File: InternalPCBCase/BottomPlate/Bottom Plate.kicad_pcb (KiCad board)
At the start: 2 copper layers, 138.6 x 93.5 mm, 6 parts

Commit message: V1.01 PCB and Plates incl Gerbers
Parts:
- added SCREW7: MountingHole_2.2mm_M2_DIN965, Mounting_Holes:MountingHole_2.2mm_M2_DIN965, F.Cu at (128.5, 106.8)
- added SCREW8: MountingHole_2.2mm_M2_DIN965, Mounting_Holes:MountingHole_2.2mm_M2_DIN965, F.Cu at (154.9, 68.8)
- moved SCREW4 4.48 mm to (154.9, 106.8)
- moved SCREW3 1.35 mm to (128.5, 68.8)
- moved SCREW5 1.06 mm to (189.2, 72.2)
- moved SCREW6 0.58 mm to (184.8, 109.2)
- moved SCREW1 0.24 mm to (94.0, 72.2)
- moved SCREW2 0.14 mm to (94.0, 110.3)
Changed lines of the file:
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@@
     (links 0)
     (no_connects 0)
-    (area 52.5 39 227.000001 157.500001)
+    (area 74.884999 46.149999 213.565001 139.745001)
     (thickness 1.6)
     (drawings 257)
     (tracks 0)
     (zones 0)
-    (modules 6)
+    (modules 8)
     (nets 1)
   )
   (page A4)
   (layers
-    (0 F.Cu signal hide)
-    (31 B.Cu signal hide)
+    (0 F.Cu signal)
+    (31 B.Cu signal)
     (32 B.Adhes user)
     (33 F.Adhes user)
@@
   )
   (module Mounting_Holes:MountingHole_2.2mm_M2_DIN965 (layer F.Cu)
-    (at 93.98 110.49)
+    (at 93.96 110.35)
     (descr "Mounting Hole 2.2mm, no annular, M2, DIN965")
     (tags "mounting hole 2.2mm no annular m2 din965")
@@
   )
   (module Mounting_Holes:MountingHole_2.2mm_M2_DIN965 (layer F.Cu)
-    (at 93.98 72.39)
+    (at 93.96 72.15)
     (descr "Mounting Hole 2.2mm, no annular, M2, DIN965")
     (tags "mounting hole 2.2mm no annular m2 din965")
@@
   )
   (module Mounting_Holes:MountingHole_2.2mm_M2_DIN965 (layer F.Cu)
-    (at 185.341 109.074)
+    (at 184.78 109.22)
     (descr "Mounting Hole 2.2mm, no annular, M2, DIN965")
     (tags "mounting hole 2.2mm no annular m2 din965")
@@
   )
   (module Mounting_Holes:MountingHole_2.2mm_M2_DIN965 (layer F.Cu)
-    (at 151.1074 104.489)
+    (at 154.91 106.85)
     (descr "Mounting Hole 2.2mm, no annular, M2, DIN965")
     (tags "mounting hole 2.2mm no annular m2 din965")
@@
       (effects (font (size 1 1) (thickness 0.15)))
     )
-    (fp_text value MountingHole_2.2mm_M2_DIN965 (at 0 2.9) (layer F.Fab)
-      (effects (font (size 1 1) (thickness 0.15)))
-    )
-    (fp_text user %R (at 0.3 0) (layer F.Fab)
-      (effects (font (size 1 1) (thickness 0.15)))
-    )
-    (fp_circle (center 0 0) (end 1.9 0) (layer Cmts.User) (width 0.15))
-    (fp_circle (center 0 0) (end 2.15 0) (layer F.CrtYd) (width 0.05))
-    (pad 1 np_thru_hole circle (at 0 0) (size 2.2 2.2) (drill 2.2) (layers *.Cu *.Mask))
-  )
-  (module Mounting_Holes:MountingHole_2.2mm_M2_DIN965 (layer F.Cu)
-    (at 189.2117 71.088)
+    (fp_text value MountingHole_2.2mm_M2_DIN965 (at 0 2.9) (layer F.Fab) hide
+      (effects (font (size 1 1) (thickness 0.15)))
+    )
+    (fp_text user %R (at 0.3 0) (layer F.Fab)
+      (effects (font (size 1 1) (thickness 0.15)))
+    )
+    (fp_circle (center 0 0) (end 1.9 0) (layer Cmts.User) (width 0.15))
+    (fp_circle (center 0 0) (end 2.15 0) (layer F.CrtYd) (width 0.05))
+    (pad 1 np_thru_hole circle (at 0 0) (size 2.2 2.2) (drill 2.2) (layers *.Cu *.Mask))
+  )
+  (module Mounting_Holes:MountingHole_2.2mm_M2_DIN965 (layer F.Cu)
+    (at 189.25 72.15)
     (descr "Mounting Hole 2.2mm, no annular, M2, DIN965")
     (tags "mounting hole 2.2mm no annular m2 din965")
@@
   )
   (module Mounting_Holes:MountingHole_2.2mm_M2_DIN965 (layer F.Cu)
-    (at 129.852 68.7068)
+    (at 128.5 68.75)
     (descr "Mounting Hole 2.2mm, no annular, M2, DIN965")
     (tags "mounting hole 2.2mm no annular m2 din965")
@@
     (pad 1 np_thru_hole circle (at 0 0) (size 2.2 2.2) (drill 2.2) (layers *.Cu *.Mask))
   )
-  (gr_text "ErgoTravel V1.01" (at 143.5 66.75) (layer F.SilkS)
+  (module Mounting_Holes:MountingHole_2.2mm_M2_DIN965 (layer F.Cu)
+    (at 128.5 106.85)
+    (descr "Mounting Hole 2.2mm, no annular, M2, DIN965")
+    (tags "mounting hole 2.2mm no annular m2 din965")
+    (attr virtual)
+    (fp_text reference SCREW7 (at 0 -2.9) (layer F.SilkS) hide
+      (effects (font (size 1 1) (thickness 0.15)))
+    )
+    (fp_text value MountingHole_2.2mm_M2_DIN965 (at 0 2.9) (layer F.Fab) hide
+      (effects (font (size 1 1) (thickness 0.15)))
+    )
+    (fp_text user %R (at 0.3 0) (layer F.Fab) hide
+      (effects (font (size 1 1) (thickness 0.15)))
+    )
+    (fp_circle (center 0 0) (end 1.9 0) (layer Cmts.User) (width 0.15))
+    (fp_circle (center 0 0) (end 2.15 0) (layer F.CrtYd) (width 0.05))
+    (pad 1 np_thru_hole circle (at 0 0) (size 2.2 2.2) (drill 2.2) (layers *.Cu *.Mask))
+  )
+  (module Mounting_Holes:MountingHole_2.2mm_M2_DIN965 (layer F.Cu)
+    (at 154.91 68.75)
+    (descr "Mounting Hole 2.2mm, no annular, M2, DIN965")
+    (tags "mounting hole 2.2mm no annular m2 din965")
+    (attr virtual)
+    (fp_text reference SCREW8 (at 0 -2.9) (layer F.SilkS) hide
+      (effects (font (size 1 1) (thickness 0.15)))
+    )
+    (fp_text value MountingHole_2.2mm_M2_DIN965 (at 0 2.9) (layer F.Fab) hide
+      (effects (font (size 1 1) (thickness 0.15)))
+    )
+    (fp_text user %R (at 0.3 0) (layer F.Fab)
+      (effects (font (size 1 1) (thickness 0.15)))
+    )
+    (fp_circle (center 0 0) (end 1.9 0) (layer Cmts.User) (width 0.15))
+    (fp_circle (center 0 0) (end 2.15 0) (layer F.CrtYd) (width 0.05))
+    (pad 1 np_thru_hole circle (at 0 0) (size 2.2 2.2) (drill 2.2) (layers *.Cu *.Mask))
+  )
+  (gr_text "ErgoTravel V1.01" (at 141.224 66.294) (layer F.SilkS)
     (effects (font (size 1.5 1.5) (thickness 0.3)))
   )
-  (gr_text JLCJLCJLCJLC (at 138.75 69) (layer F.SilkS)
-    (effects (font (size 1 1) (thickness 0.1)))
+  (gr_text JLCJLCJLCJLC (at 141.224 68.453) (layer F.SilkS)
+    (effects (font (size 0.6 0.6) (thickness 0.1)))
   )
   (gr_line (start 206.284 46.3926) (end 206.308 46.4015) (layer Edge.Cuts) (width 0.1))

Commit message: initial V1.02 files and 3d printed case folders
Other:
- board text added: "ErgoTravel V1.02"
- board text removed: "ErgoTravel V1.01"
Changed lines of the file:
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@@
     (links 0)
     (no_connects 0)
-    (area 74.884999 46.149999 213.565001 139.745001)
+    (area 52.5 39 227.000001 157.500001)
     (thickness 1.6)
     (drawings 257)
@@
   (page A4)
   (layers
-    (0 F.Cu signal)
-    (31 B.Cu signal)
+    (0 F.Cu signal hide)
+    (31 B.Cu signal hide)
     (32 B.Adhes user)
     (33 F.Adhes user)
@@
     (pad 1 np_thru_hole circle (at 0 0) (size 2.2 2.2) (drill 2.2) (layers *.Cu *.Mask))
   )
-  (gr_text "ErgoTravel V1.01" (at 141.224 66.294) (layer F.SilkS)
+  (gr_text "ErgoTravel V1.02" (at 141.224 66.294) (layer F.SilkS)
     (effects (font (size 1.5 1.5) (thickness 0.3)))
   )
-  (gr_text JLCJLCJLCJLC (at 141.224 68.453) (layer F.SilkS)
+  (gr_text JLCJLCJLCJLC (at 136.779 68.326) (layer F.SilkS)
     (effects (font (size 0.6 0.6) (thickness 0.1)))
   )

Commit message: updating Internal Plates Gerbers
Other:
- board text added: "ErgoTravel V1.03"
- board text removed: "ErgoTravel V1.02"
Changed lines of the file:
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@@
     (pad 1 np_thru_hole circle (at 0 0) (size 2.2 2.2) (drill 2.2) (layers *.Cu *.Mask))
   )
-  (gr_text "ErgoTravel V1.02" (at 141.224 66.294) (layer F.SilkS)
+  (gr_text "ErgoTravel V1.03" (at 141.224 66.294) (layer F.SilkS)
     (effects (font (size 1.5 1.5) (thickness 0.3)))
   )

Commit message: last Kicad4.7 commit
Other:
- board text added: "ErgoTravel"
- board text removed: "ErgoTravel V1.03"
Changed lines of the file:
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@@
     (pad 1 np_thru_hole circle (at 0 0) (size 2.2 2.2) (drill 2.2) (layers *.Cu *.Mask))
   )
-  (gr_text "ErgoTravel V1.03" (at 141.224 66.294) (layer F.SilkS)
+  (gr_text ErgoTravel (at 139.192 66.548) (layer F.SilkS)
     (effects (font (size 1.5 1.5) (thickness 0.3)))
   )

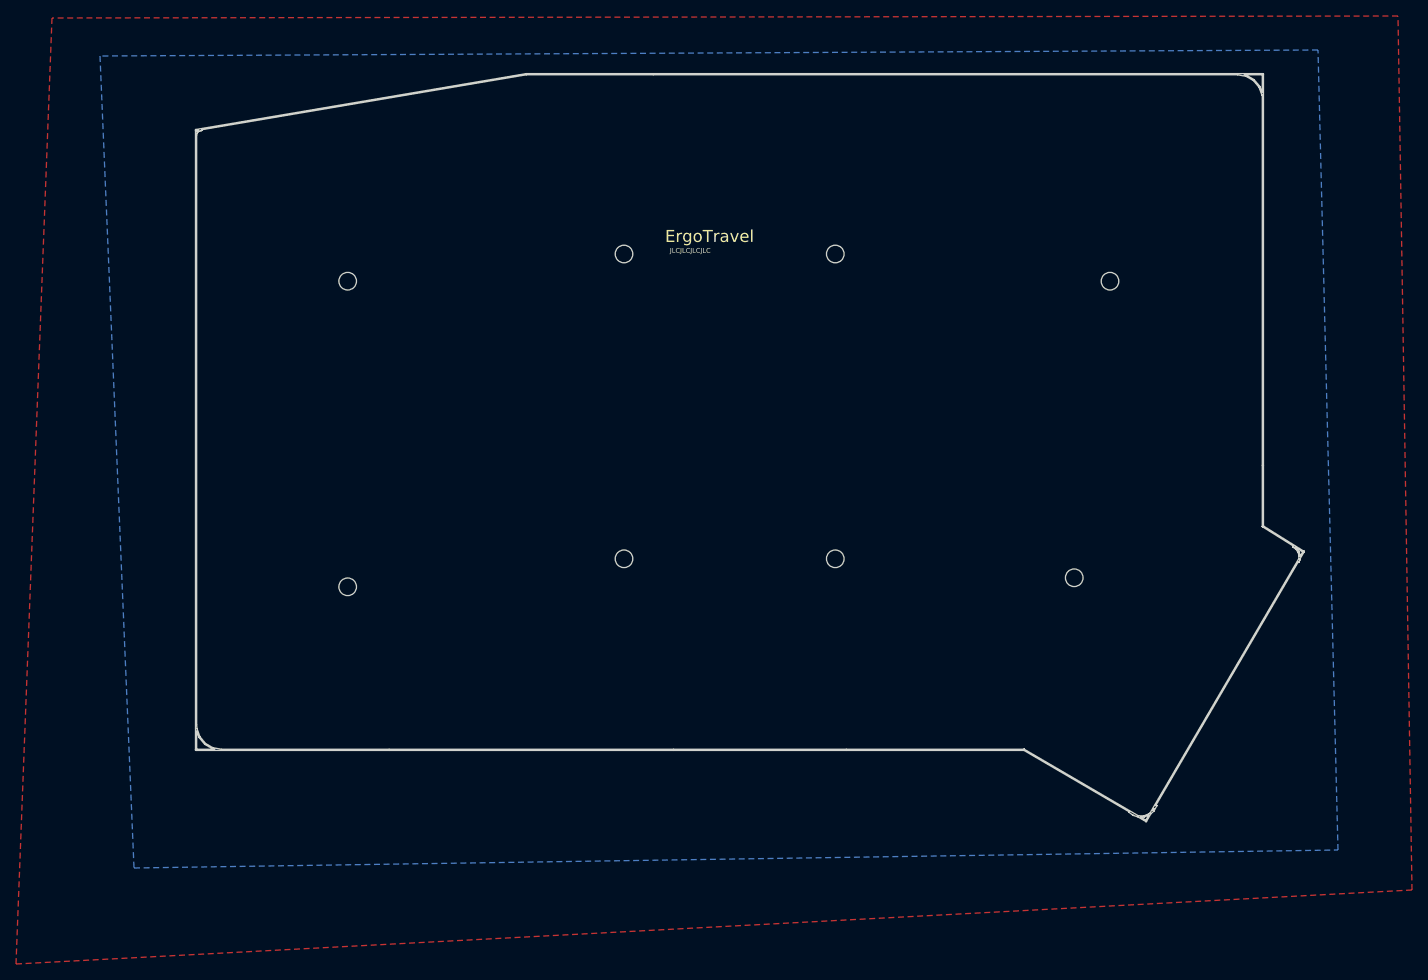
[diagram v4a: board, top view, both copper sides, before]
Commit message: added MX version (V1.1) to avoid extra JLCPCB fees
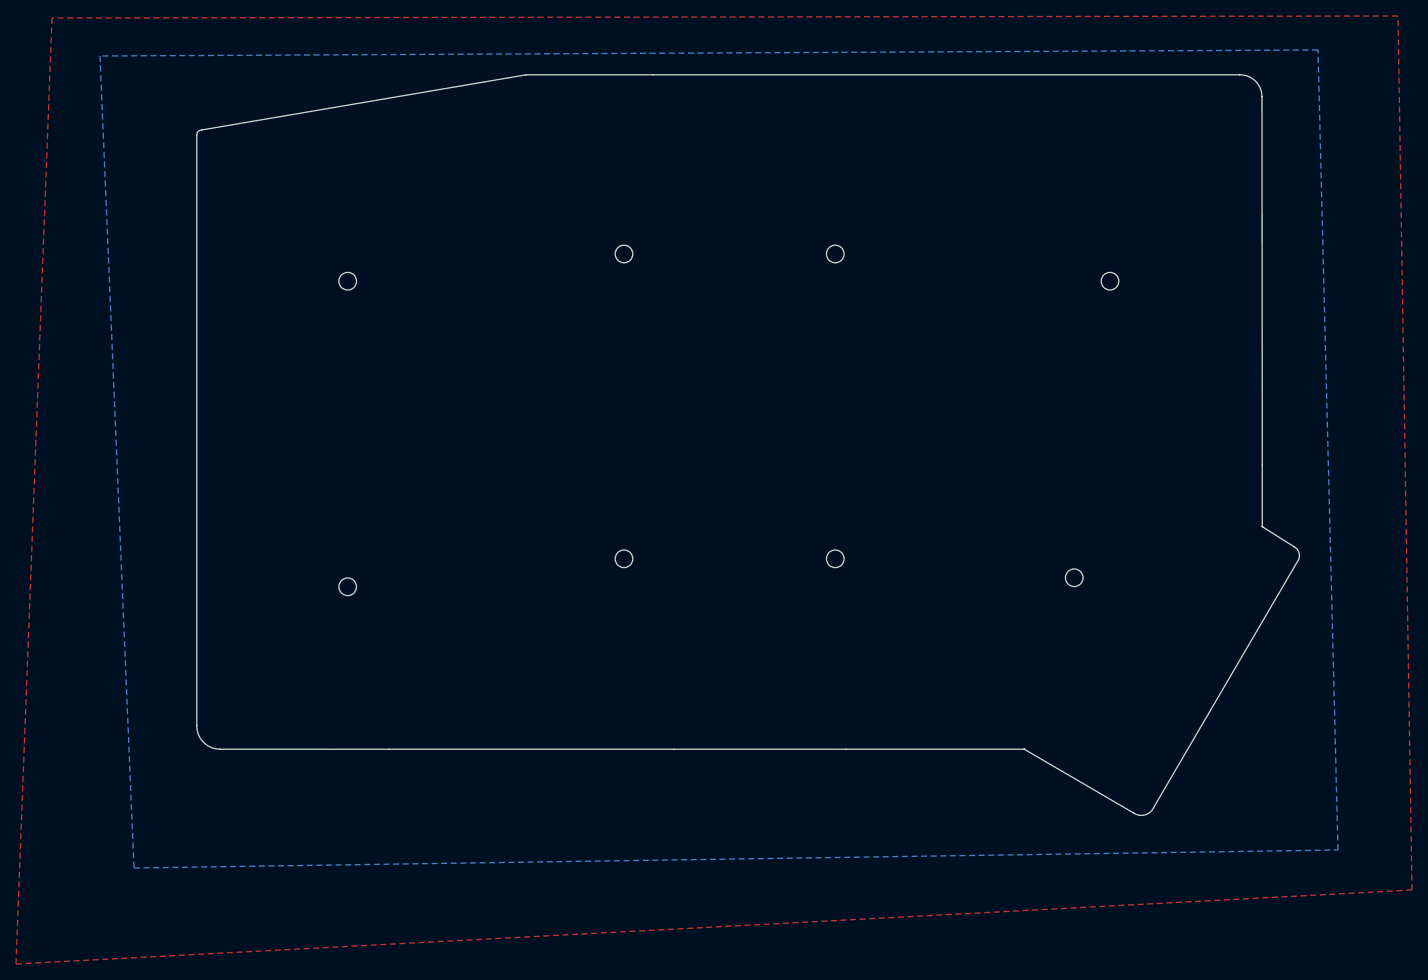
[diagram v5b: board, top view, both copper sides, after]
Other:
- board size 138.6 x 93.5 mm -> 137.8 x 92.6 mm
- board text removed: "ErgoTravel"
- board text removed: "JLCJLCJLCJLC"
